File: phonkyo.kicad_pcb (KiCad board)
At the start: 2 copper layers, 65 x 30 mm, 31 parts, among them J1 GPIO, J2 LineOutJack, J4 RIJack, U2 PCM5102A, U3 XC6206P332MR

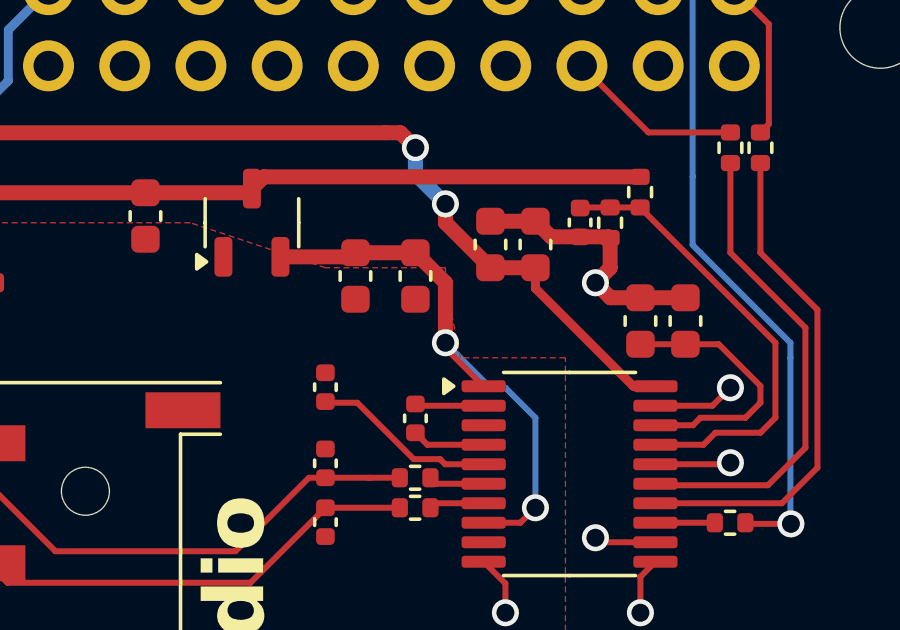
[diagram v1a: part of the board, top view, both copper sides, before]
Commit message: pcb: move C7 to sit directly at U2 pin 1 (CPVDD)
C7 is the 100 nF decoupling cap on the PCM5102A's charge-pump supply,
CPVDD (pin 1). Per the datasheet, pin 1 is CPVDD rather than AVDD. C7
was at (146.0, 81.8), 3.7 mm from the pin and reached by a track that
ran down to a via beside the chip. The datasheet asks for supply and
charge-pump decoupling "as close as possible to the device".

C7 now sits horizontally at (147.65, 84.0). Its +3.3VA pad is directly
above pin 1, 0.75 mm pad-to-pad, and its GNDA pad lands inside the
analog pour.

The +3.3VA via at (147, 84) would have fallen under C7's GNDA pad, so
it moves to (147.7, 82.7), off the pad (no via-in-pad). The B.Cu run on
to pin 8 (AVDD) is rejoined from the new via position.

Semantic diff against the previous board: one footprint moved (C7), no
footprints added or removed, and 5 tracks/vias replaced by 7, all on
+3.3VA. DRC with schematic parity matches the baseline: 0 unconnected,
0 parity errors, no new violations.

Zones were refilled by KiCad 10, so the stored fill polygons also
change.

Co-Authored-By: Claude Opus 5.5 <noreply@anthropic.com>
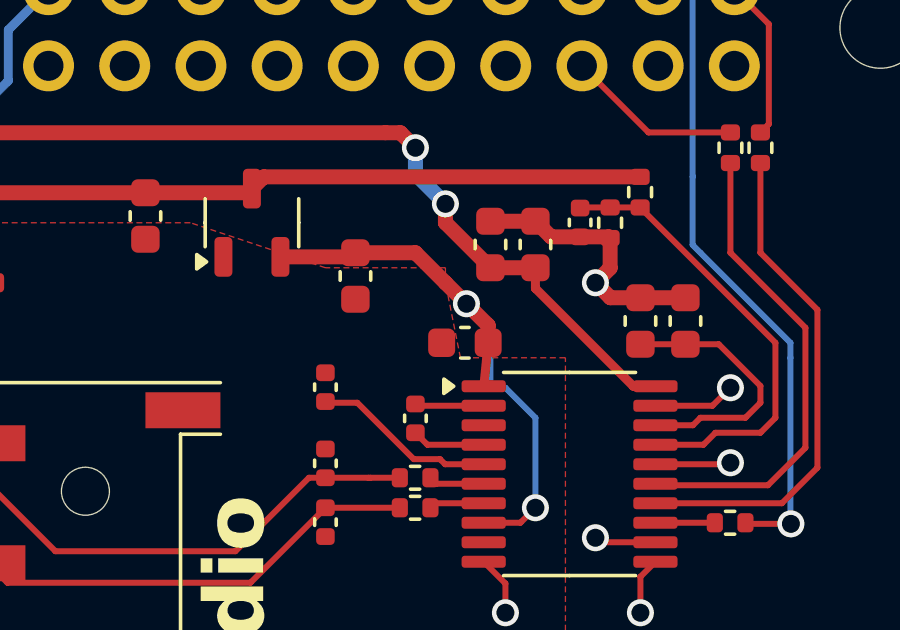
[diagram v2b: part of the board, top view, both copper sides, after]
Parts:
- moved C7 2.77 mm to (147.7, 84.0), turned to 0 degrees
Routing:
- net +3.3VA: track 18.9 -> 20.0 mm
